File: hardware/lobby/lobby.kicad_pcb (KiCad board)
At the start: 4 copper layers, 85 x 56 mm, 38 parts, among them J1 THD-02-R, J2 THD-20-R, J3 Micro_SD_Card_Det, J4 Conn_01x22_Female, SW1 SW_Push, SW2 SW_SPST, U1 RT9742GGJ5, U2 M.2-keyM, U3 MYLSM00502ERPL, U4 FSUSB42MX

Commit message: update lobby
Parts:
- added H1: MountingHole, MountingHole:MountingHole_2.7mm_M2.5, F.Cu at (69.8, 63.0)
- added H2: MountingHole, MountingHole:MountingHole_2.7mm_M2.5, F.Cu at (100.0, 63.0)
- J3: footprint cm4crypto:SDCARD_MOLEX_503398-1892 -> cm4crypto:amphenol-sd-push-pull_114-00841-68
- R3, R4: value nf -> 2.2K
- R5: value 12K 1% -> nf
- R6: value 2.2k -> nf
- R7: value R -> 12K 1%
- R8: value 2.2K -> 2.2k
- R9: value 2.2K -> R
- moved R8 61.1 mm to (25.0, 31.5)
- moved R6 39.6 mm to (62.0, 45.5), turned to 180 degrees
- moved R3 30.6 mm to (86.0, 28.0), turned to 90 degrees
- moved R4 28.5 mm to (84.5, 28.0), turned to 90 degrees
- moved R9 18.4 mm to (69.8, 39.0), turned to -90 degrees
- moved R7 8.84 mm to (62.0, 43.2), turned to 0 degrees
- moved J3 6.79 mm to (22.8, 47.9), turned to 90 degrees
- moved R5 3.75 mm to (62.0, 47.0), turned to 180 degrees
- moved U2 0.56 mm to (26.2, 63.0)
- moved C10 0.55 mm to (35.5, 72.5)
- moved C4 0.55 mm to (34.0, 72.5)
- moved C5 0.55 mm to (32.5, 72.5)
- moved C11 0.55 mm to (31.0, 72.5)
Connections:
- Module1 pad 100: unconnected-(Module1-Pad100) -> (no net)
- Module1 pad 104: unconnected-(Module1-Pad104) -> (no net)
- Module1 pad 106: unconnected-(Module1-Pad106) -> (no net)
- Module1 pad 111: unconnected-(Module1-Pad111) -> (no net)
- Module1 pad 128: unconnected-(Module1-Pad128) -> (no net)
- Module1 pad 130: unconnected-(Module1-Pad130) -> (no net)
- Module1 pad 134: unconnected-(Module1-Pad134) -> (no net)
- Module1 pad 136: unconnected-(Module1-Pad136) -> (no net)
- Module1 pad 140: unconnected-(Module1-Pad140) -> (no net)
- Module1 pad 142: unconnected-(Module1-Pad142) -> (no net)
- Module1 pad 157: unconnected-(Module1-Pad157) -> (no net)
- Module1 pad 159: unconnected-(Module1-Pad159) -> (no net)
- Module1 pad 16: unconnected-(Module1-Pad16) -> (no net)
- Module1 pad 163: unconnected-(Module1-Pad163) -> (no net)
- Module1 pad 165: unconnected-(Module1-Pad165) -> (no net)
- Module1 pad 169: unconnected-(Module1-Pad169) -> (no net)
- Module1 pad 171: unconnected-(Module1-Pad171) -> (no net)
- Module1 pad 175: unconnected-(Module1-Pad175) -> (no net)
- Module1 pad 177: unconnected-(Module1-Pad177) -> (no net)
- Module1 pad 18: unconnected-(Module1-Pad18) -> (no net)
- Module1 pad 181: unconnected-(Module1-Pad181) -> (no net)
- Module1 pad 183: unconnected-(Module1-Pad183) -> (no net)
- Module1 pad 187: unconnected-(Module1-Pad187) -> (no net)
- Module1 pad 189: unconnected-(Module1-Pad189) -> (no net)
- Module1 pad 19: unconnected-(Module1-Pad19) -> (no net)
- Module1 pad 193: unconnected-(Module1-Pad193) -> (no net)
- Module1 pad 194: unconnected-(Module1-Pad194) -> (no net)
- Module1 pad 195: unconnected-(Module1-Pad195) -> (no net)
- Module1 pad 196: unconnected-(Module1-Pad196) -> (no net)
- Module1 pad 24: /GPIO26 -> (no net)
- Module1 pad 25: /GPIO21 -> (no net)
- Module1 pad 26: /GPIO19 -> (no net)
- Module1 pad 27: /GPIO20 -> (no net)
- Module1 pad 28: /GPIO13 -> (no net)
- Module1 pad 29: /GPIO16 -> (no net)
- Module1 pad 30: /GPIO6 -> (no net)
- Module1 pad 31: /GPIO12 -> (no net)
- Module1 pad 34: /GPIO5 -> (no net)
- Module1 pad 35: /ID_SC -> (no net)
- Module1 pad 36: /ID_SD -> (no net)
- Module1 pad 37: /GPIO7 -> (no net)
- Module1 pad 38: /GPIO11 -> (no net)
- Module1 pad 39: /GPIO8 -> (no net)
- Module1 pad 40: /GPIO9 -> (no net)
- Module1 pad 41: /GPIO25 -> (no net)
- Module1 pad 44: /GPIO10 -> (no net)
- Module1 pad 45: /GPIO24 -> (no net)
- Module1 pad 46: /GPIO22 -> (no net)
- Module1 pad 47: /GPIO23 -> (no net)
- Module1 pad 48: /GPIO27 -> (no net)
- Module1 pad 49: /GPIO18 -> (no net)
- Module1 pad 50: /GPIO17 -> (no net)
- Module1 pad 51: /GPIO15 -> (no net)
- Module1 pad 54: /GPIO4 -> (no net)
- Module1 pad 64: unconnected-(Module1-Pad64) -> (no net)
- Module1 pad 68: unconnected-(Module1-Pad68) -> (no net)
- Module1 pad 70: unconnected-(Module1-Pad70) -> (no net)
- Module1 pad 72: unconnected-(Module1-Pad72) -> (no net)
- Module1 pad 73: unconnected-(Module1-Pad73) -> (no net)
- Module1 pad 76: unconnected-(Module1-Pad76) -> (no net)
- Module1 pad 84: unconnected-(Module1-Pad84) -> (no net)
- Module1 pad 86: unconnected-(Module1-Pad86) -> (no net)
- Module1 pad 92: unconnected-(Module1-Pad92) -> (no net)
- Module1 pad 99: unconnected-(Module1-Pad99) -> (no net)
- R3 pad 1: /+3.3v -> /GPIO_VREF
- R3 pad 2: Net-(J3-Pad10) -> /GPIO2
- R4 pad 1: (no net) -> /GPIO_VREF
- R4 pad 2: Net-(J3-Pad9) -> /GPIO3
- R5 pad 2: /SD_PWR_ON -> Net-(J3-Pad10)
- R6 pad 1: /USBOTG_ID -> (no net)
- R6 pad 2: GND -> Net-(J3-Pad9)
- R7 pad 1: Net-(R7-Pad1) -> /+3.3v
- R7 pad 2: GND -> /SD_PWR_ON
- R8 pad 1: /GPIO_VREF -> /USBOTG_ID
- R8 pad 2: /GPIO2 -> GND
- R9 pad 1: /GPIO_VREF -> Net-(R9-Pad1)
- R9 pad 2: /GPIO3 -> GND
- U3 pad 1: Net-(R7-Pad1) -> Net-(R9-Pad1)
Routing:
- net GND: track 148.5 -> 126.0 mm, vias 195 -> 187
- net Net-(R7-Pad1): track 17.0 -> 0.00 mm, vias 2 -> 0
- net Net-(R9-Pad1): track 0.00 -> 16.8 mm, vias 0 -> 2
- net /+3.3v: track 240.5 -> 230.4 mm, vias 10 -> 13
- net Net-(J3-Pad10): track 33.9 -> 42.8 mm
- net /TR1_TAP: track 63.2 -> 71.6 mm
- net Net-(J3-Pad9): track 30.6 -> 38.3 mm
- net /TR0_TAP: track 78.5 -> 85.9 mm
- net /TR2_TAP: track 72.9 -> 80.1 mm
- net /SD_DAT0: track 72.2 -> 79.1 mm
- net /TR3_TAP: track 79.5 -> 83.6 mm
- net /+5v: track 167.8 -> 171.8 mm
- net /SD_CLK: track 65.2 -> 69.0 mm
- net /SD_DAT2: track 69.2 -> 72.9 mm
- net /sd/SD_PWR: track 50.8 -> 47.6 mm
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- added copper zone on B.Cu, net /+3.3v

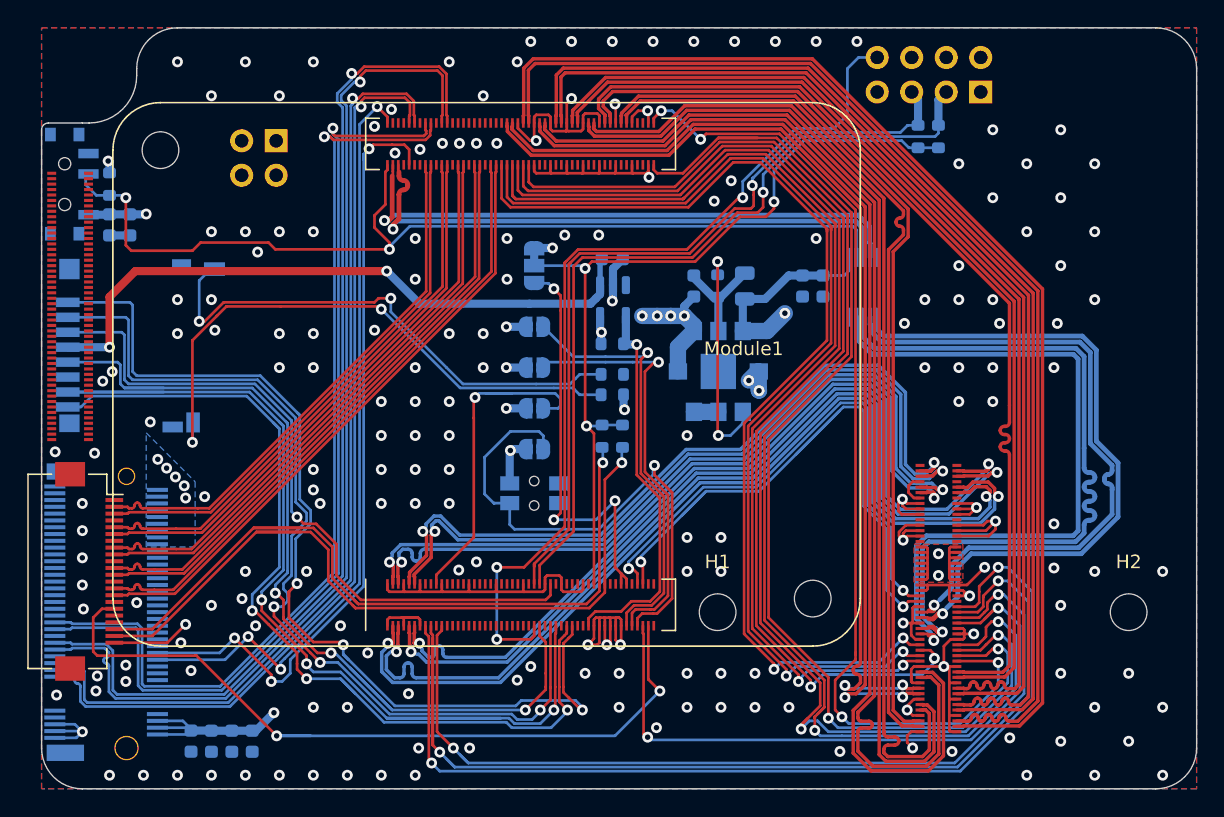
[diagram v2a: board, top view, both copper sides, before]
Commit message: mirror lobby mezzanine connector
fixing a big whoops
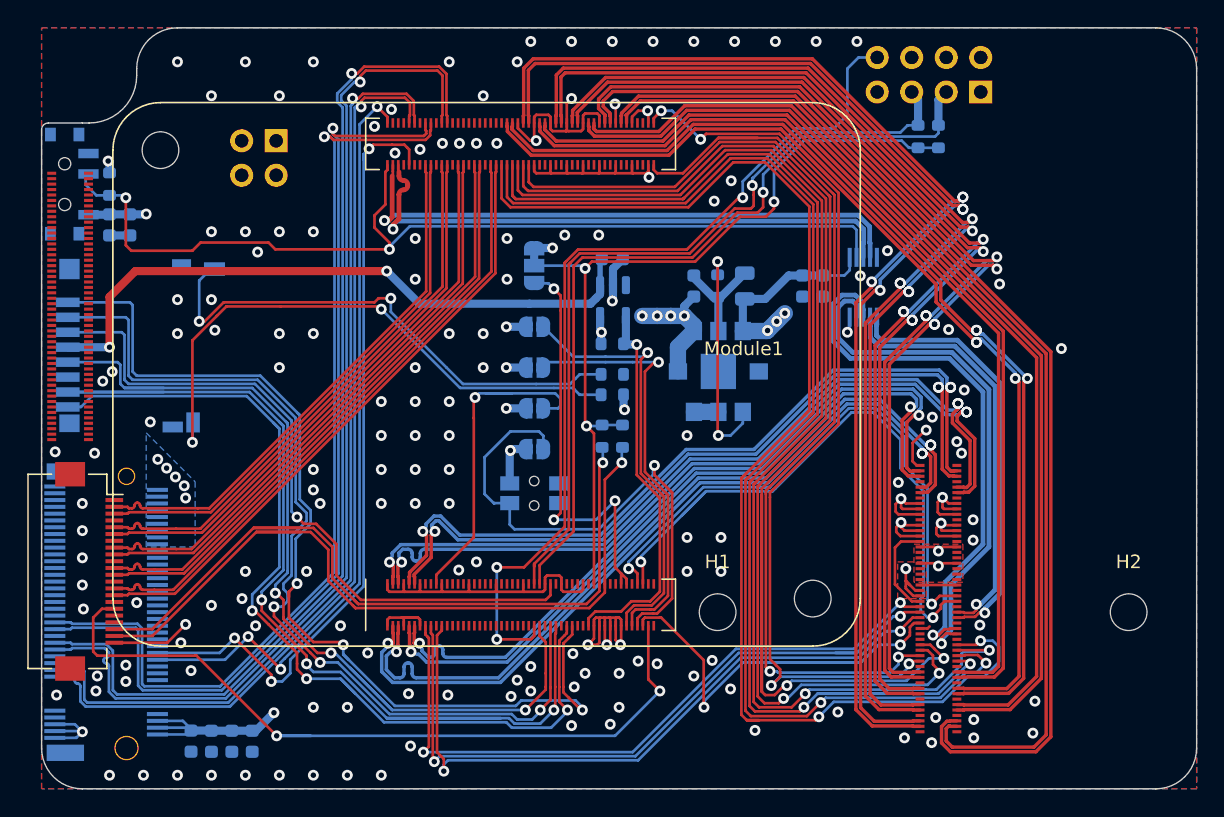
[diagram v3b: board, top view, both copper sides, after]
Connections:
- J4 pad 18: (no net) -> unconnected-(J4-Pad18)
- Module1 pad 100: (no net) -> unconnected-(Module1-Pad100)
- Module1 pad 104: (no net) -> unconnected-(Module1-Pad104)
- Module1 pad 106: (no net) -> unconnected-(Module1-Pad106)
- Module1 pad 111: (no net) -> unconnected-(Module1-Pad111)
- Module1 pad 128: (no net) -> unconnected-(Module1-Pad128)
- Module1 pad 130: (no net) -> unconnected-(Module1-Pad130)
- Module1 pad 134: (no net) -> unconnected-(Module1-Pad134)
- Module1 pad 136: (no net) -> unconnected-(Module1-Pad136)
- Module1 pad 140: (no net) -> unconnected-(Module1-Pad140)
- Module1 pad 142: (no net) -> unconnected-(Module1-Pad142)
- Module1 pad 157: (no net) -> unconnected-(Module1-Pad157)
- Module1 pad 159: (no net) -> unconnected-(Module1-Pad159)
- Module1 pad 16: (no net) -> unconnected-(Module1-Pad16)
- Module1 pad 163: (no net) -> unconnected-(Module1-Pad163)
- Module1 pad 165: (no net) -> unconnected-(Module1-Pad165)
- Module1 pad 169: (no net) -> unconnected-(Module1-Pad169)
- Module1 pad 171: (no net) -> unconnected-(Module1-Pad171)
- Module1 pad 175: (no net) -> unconnected-(Module1-Pad175)
- Module1 pad 177: (no net) -> unconnected-(Module1-Pad177)
- Module1 pad 18: (no net) -> unconnected-(Module1-Pad18)
- Module1 pad 181: (no net) -> unconnected-(Module1-Pad181)
- Module1 pad 183: (no net) -> unconnected-(Module1-Pad183)
- Module1 pad 187: (no net) -> unconnected-(Module1-Pad187)
- Module1 pad 189: (no net) -> unconnected-(Module1-Pad189)
- Module1 pad 19: (no net) -> unconnected-(Module1-Pad19)
- Module1 pad 193: (no net) -> unconnected-(Module1-Pad193)
- Module1 pad 194: (no net) -> unconnected-(Module1-Pad194)
- Module1 pad 195: (no net) -> unconnected-(Module1-Pad195)
- Module1 pad 196: (no net) -> unconnected-(Module1-Pad196)
- Module1 pad 24: (no net) -> /GPIO26
- Module1 pad 25: (no net) -> /GPIO21
- Module1 pad 26: (no net) -> /GPIO19
- Module1 pad 27: (no net) -> /GPIO20
- Module1 pad 28: (no net) -> /GPIO13
- Module1 pad 29: (no net) -> /GPIO16
- Module1 pad 30: (no net) -> /GPIO6
- Module1 pad 31: (no net) -> /GPIO12
- Module1 pad 34: (no net) -> /GPIO5
- Module1 pad 35: (no net) -> /ID_SC
- Module1 pad 36: (no net) -> /ID_SD
- Module1 pad 37: (no net) -> /GPIO7
- Module1 pad 38: (no net) -> /GPIO11
- Module1 pad 39: (no net) -> /GPIO8
- Module1 pad 40: (no net) -> /GPIO9
- Module1 pad 41: (no net) -> /GPIO25
- Module1 pad 44: (no net) -> /GPIO10
- Module1 pad 45: (no net) -> /GPIO24
- Module1 pad 46: (no net) -> /GPIO22
- Module1 pad 47: (no net) -> /GPIO23
- Module1 pad 48: (no net) -> /GPIO27
- Module1 pad 49: (no net) -> /GPIO18
- Module1 pad 50: (no net) -> /GPIO17
- Module1 pad 51: (no net) -> /GPIO15
- Module1 pad 54: (no net) -> /GPIO4
- Module1 pad 64: (no net) -> unconnected-(Module1-Pad64)
- Module1 pad 68: (no net) -> unconnected-(Module1-Pad68)
- Module1 pad 70: (no net) -> unconnected-(Module1-Pad70)
- Module1 pad 72: (no net) -> unconnected-(Module1-Pad72)
- Module1 pad 73: (no net) -> unconnected-(Module1-Pad73)
- Module1 pad 76: (no net) -> unconnected-(Module1-Pad76)
- Module1 pad 84: (no net) -> unconnected-(Module1-Pad84)
- Module1 pad 86: (no net) -> unconnected-(Module1-Pad86)
- Module1 pad 92: (no net) -> unconnected-(Module1-Pad92)
- Module1 pad 99: (no net) -> unconnected-(Module1-Pad99)
- Module2 pad 10: /TRD3_P -> /TRD1_P
- Module2 pad 11: /TRD1_N -> /TRD3_N
- Module2 pad 12: /TRD3_N -> /TRD1_N
- Module2 pad 15: /TR1_TAP -> /TR3_TAP
- Module2 pad 16: /TR3_TAP -> /TR1_TAP
- Module2 pad 17: /TR1_TAP -> /TR3_TAP
- Module2 pad 18: /TR3_TAP -> /TR1_TAP
- Module2 pad 19: /TR1_TAP -> /TR3_TAP
- Module2 pad 20: /TR3_TAP -> /TR1_TAP
- Module2 pad 23: /TR2_TAP -> /TR0_TAP
- Module2 pad 24: /TR0_TAP -> /TR2_TAP
- Module2 pad 25: /TR2_TAP -> /TR0_TAP
- Module2 pad 26: /TR0_TAP -> /TR2_TAP
- Module2 pad 27: /TR2_TAP -> /TR0_TAP
- Module2 pad 28: /TR0_TAP -> /TR2_TAP
- Module2 pad 3: /TRD0_N -> /TRD2_P
- Module2 pad 4: /TRD2_P -> /TRD0_N
- Module2 pad 47: GND -> /+3.3v
- Module2 pad 48: /+3.3v -> GND
- Module2 pad 49: /AnalogIP1 -> /+3.3v
- Module2 pad 5: /TRD0_P -> /TRD2_N
- Module2 pad 50: /+3.3v -> /AnalogIP1
- Module2 pad 51: /AnalogIP0 -> GND
- Module2 pad 52: GND -> /AnalogIP0
- Module2 pad 53: GND -> /ETH_LEDY
- Module2 pad 54: /ETH_LEDY -> GND
- Module2 pad 55: /USB2_HOST_P -> /ETH_LEDG
- Module2 pad 56: /ETH_LEDG -> /USB2_HOST_P
- Module2 pad 57: /USB2_HOST_N -> /nPI_LED_ACTIVITY
- Module2 pad 58: /nPI_LED_ACTIVITY -> /USB2_HOST_N
- Module2 pad 59: GND -> /nPI_LED_PWR
- Module2 pad 6: /TRD2_N -> /TRD0_P
- Module2 pad 60: /nPI_LED_PWR -> GND
- Module2 pad 61: /USB2_DEV_N -> GND
- Module2 pad 62: GND -> /USB2_DEV_N
- Module2 pad 63: /USB2_DEV_P -> GND
- Module2 pad 64: GND -> /USB2_DEV_P
- Module2 pad 67: /HDMI1_HOTPLUG -> /HDMI0_HOTPLUG
- Module2 pad 68: /HDMI0_HOTPLUG -> /HDMI1_HOTPLUG
- Module2 pad 69: /HDMI1_CEC -> /HDMI0_CEC
- Module2 pad 70: /HDMI0_CEC -> /HDMI1_CEC
- Module2 pad 71: /HDMI1_SDA -> /HDMI0_SDA
- Module2 pad 72: /HDMI0_SDA -> /HDMI1_SDA
- Module2 pad 73: /HDMI1_SCL -> /HDMI0_SCL
- Module2 pad 74: /HDMI0_SCL -> /HDMI1_SCL
- Module2 pad 77: /HDMI1_TX0_P -> /HDMI0_TX0_N
- Module2 pad 78: /HDMI0_TX0_N -> /HDMI1_TX0_P
- Module2 pad 79: /HDMI1_TX0_N -> /HDMI0_TX0_P
- Module2 pad 80: /HDMI0_TX0_P -> /HDMI1_TX0_N
- Module2 pad 83: /HDMI1_TX2_P -> /HDMI0_TX2_N
- Module2 pad 84: /HDMI0_TX2_N -> /HDMI1_TX2_P
- Module2 pad 85: /HDMI1_TX2_N -> /HDMI0_TX2_P
- Module2 pad 86: /HDMI0_TX2_P -> /HDMI1_TX2_N
- Module2 pad 89: /HDMI0_TX1_P -> /HDMI1_CLK_N
- Module2 pad 9: /TRD1_P -> /TRD3_P
- Module2 pad 90: /HDMI1_CLK_N -> /HDMI0_TX1_P
- Module2 pad 91: /HDMI0_TX1_N -> /HDMI1_CLK_P
- Module2 pad 92: /HDMI1_CLK_P -> /HDMI0_TX1_N
- Module2 pad 95: /HDMI0_CLK_P -> /HDMI1_TX1_N
- Module2 pad 96: /HDMI1_TX1_N -> /HDMI0_CLK_P
- Module2 pad 97: /HDMI0_CLK_N -> /HDMI1_TX1_P
- Module2 pad 98: /HDMI1_TX1_P -> /HDMI0_CLK_N
- Module3 pad 1: (no net) -> unconnected-(Module3-Pad1)
- Module3 pad 10: (no net) -> unconnected-(Module3-Pad10)
- Module3 pad 100: (no net) -> unconnected-(Module3-Pad100)
- Module3 pad 11: (no net) -> unconnected-(Module3-Pad11)
- Module3 pad 12: (no net) -> unconnected-(Module3-Pad12)
- Module3 pad 13: (no net) -> unconnected-(Module3-Pad13)
- Module3 pad 14: (no net) -> unconnected-(Module3-Pad14)
- Module3 pad 15: (no net) -> unconnected-(Module3-Pad15)
- Module3 pad 16: (no net) -> unconnected-(Module3-Pad16)
- Module3 pad 17: (no net) -> unconnected-(Module3-Pad17)
- Module3 pad 18: (no net) -> unconnected-(Module3-Pad18)
- Module3 pad 19: (no net) -> unconnected-(Module3-Pad19)
- Module3 pad 2: (no net) -> unconnected-(Module3-Pad2)
- Module3 pad 20: (no net) -> unconnected-(Module3-Pad20)
- Module3 pad 21: (no net) -> unconnected-(Module3-Pad21)
- Module3 pad 22: (no net) -> unconnected-(Module3-Pad22)
- Module3 pad 23: (no net) -> unconnected-(Module3-Pad23)
- Module3 pad 24: (no net) -> unconnected-(Module3-Pad24)
- Module3 pad 25: (no net) -> unconnected-(Module3-Pad25)
- Module3 pad 26: (no net) -> unconnected-(Module3-Pad26)
- Module3 pad 27: (no net) -> unconnected-(Module3-Pad27)
- Module3 pad 28: (no net) -> unconnected-(Module3-Pad28)
- Module3 pad 29: (no net) -> unconnected-(Module3-Pad29)
- Module3 pad 3: (no net) -> unconnected-(Module3-Pad3)
- Module3 pad 30: (no net) -> unconnected-(Module3-Pad30)
- Module3 pad 31: (no net) -> unconnected-(Module3-Pad31)
- Module3 pad 32: (no net) -> unconnected-(Module3-Pad32)
- Module3 pad 33: (no net) -> unconnected-(Module3-Pad33)
- Module3 pad 34: (no net) -> unconnected-(Module3-Pad34)
- Module3 pad 35: (no net) -> unconnected-(Module3-Pad35)
- Module3 pad 36: (no net) -> unconnected-(Module3-Pad36)
- Module3 pad 37: (no net) -> unconnected-(Module3-Pad37)
- Module3 pad 38: (no net) -> unconnected-(Module3-Pad38)
- Module3 pad 39: (no net) -> unconnected-(Module3-Pad39)
- Module3 pad 4: (no net) -> unconnected-(Module3-Pad4)
- Module3 pad 40: (no net) -> unconnected-(Module3-Pad40)
- Module3 pad 41: (no net) -> unconnected-(Module3-Pad41)
- Module3 pad 42: (no net) -> unconnected-(Module3-Pad42)
- Module3 pad 43: (no net) -> unconnected-(Module3-Pad43)
- Module3 pad 44: (no net) -> unconnected-(Module3-Pad44)
- Module3 pad 45: (no net) -> unconnected-(Module3-Pad45)
- Module3 pad 46: (no net) -> unconnected-(Module3-Pad46)
- Module3 pad 47: (no net) -> unconnected-(Module3-Pad47)
- Module3 pad 48: (no net) -> unconnected-(Module3-Pad48)
- Module3 pad 49: (no net) -> unconnected-(Module3-Pad49)
- Module3 pad 5: (no net) -> unconnected-(Module3-Pad5)
- Module3 pad 50: (no net) -> unconnected-(Module3-Pad50)
- Module3 pad 51: (no net) -> unconnected-(Module3-Pad51)
- Module3 pad 52: (no net) -> unconnected-(Module3-Pad52)
- Module3 pad 53: (no net) -> unconnected-(Module3-Pad53)
- Module3 pad 54: (no net) -> unconnected-(Module3-Pad54)
- Module3 pad 55: (no net) -> unconnected-(Module3-Pad55)
- Module3 pad 56: (no net) -> unconnected-(Module3-Pad56)
- Module3 pad 57: (no net) -> unconnected-(Module3-Pad57)
- Module3 pad 58: (no net) -> unconnected-(Module3-Pad58)
- Module3 pad 59: (no net) -> unconnected-(Module3-Pad59)
- Module3 pad 6: (no net) -> unconnected-(Module3-Pad6)
- Module3 pad 60: (no net) -> unconnected-(Module3-Pad60)
- Module3 pad 61: (no net) -> unconnected-(Module3-Pad61)
- Module3 pad 62: (no net) -> unconnected-(Module3-Pad62)
- Module3 pad 63: (no net) -> unconnected-(Module3-Pad63)
- Module3 pad 64: (no net) -> unconnected-(Module3-Pad64)
- Module3 pad 65: (no net) -> unconnected-(Module3-Pad65)
- Module3 pad 66: (no net) -> unconnected-(Module3-Pad66)
- Module3 pad 67: (no net) -> unconnected-(Module3-Pad67)
- Module3 pad 68: (no net) -> unconnected-(Module3-Pad68)
- Module3 pad 69: (no net) -> unconnected-(Module3-Pad69)
- Module3 pad 7: (no net) -> unconnected-(Module3-Pad7)
- Module3 pad 70: (no net) -> unconnected-(Module3-Pad70)
- Module3 pad 71: (no net) -> unconnected-(Module3-Pad71)
- Module3 pad 72: (no net) -> unconnected-(Module3-Pad72)
- Module3 pad 73: (no net) -> unconnected-(Module3-Pad73)
- Module3 pad 74: (no net) -> unconnected-(Module3-Pad74)
- Module3 pad 75: (no net) -> unconnected-(Module3-Pad75)
- Module3 pad 76: (no net) -> unconnected-(Module3-Pad76)
- Module3 pad 77: (no net) -> unconnected-(Module3-Pad77)
- Module3 pad 78: (no net) -> unconnected-(Module3-Pad78)
- Module3 pad 79: (no net) -> unconnected-(Module3-Pad79)
- Module3 pad 8: (no net) -> unconnected-(Module3-Pad8)
- Module3 pad 80: (no net) -> unconnected-(Module3-Pad80)
- Module3 pad 81: (no net) -> unconnected-(Module3-Pad81)
- Module3 pad 82: (no net) -> unconnected-(Module3-Pad82)
- Module3 pad 83: (no net) -> unconnected-(Module3-Pad83)
- Module3 pad 84: (no net) -> unconnected-(Module3-Pad84)
- Module3 pad 85: (no net) -> unconnected-(Module3-Pad85)
- Module3 pad 86: (no net) -> unconnected-(Module3-Pad86)
- Module3 pad 87: (no net) -> unconnected-(Module3-Pad87)
- Module3 pad 88: (no net) -> unconnected-(Module3-Pad88)
- Module3 pad 89: (no net) -> unconnected-(Module3-Pad89)
- Module3 pad 9: (no net) -> unconnected-(Module3-Pad9)
- Module3 pad 90: (no net) -> unconnected-(Module3-Pad90)
- Module3 pad 91: (no net) -> unconnected-(Module3-Pad91)
- Module3 pad 92: (no net) -> unconnected-(Module3-Pad92)
- Module3 pad 93: (no net) -> unconnected-(Module3-Pad93)
- Module3 pad 94: (no net) -> unconnected-(Module3-Pad94)
- Module3 pad 95: (no net) -> unconnected-(Module3-Pad95)
- Module3 pad 96: (no net) -> unconnected-(Module3-Pad96)
- Module3 pad 97: (no net) -> unconnected-(Module3-Pad97)
- Module3 pad 98: (no net) -> unconnected-(Module3-Pad98)
- Module3 pad 99: (no net) -> unconnected-(Module3-Pad99)
- R6 pad 1: (no net) -> /sd/Reserved
- U1 pad 3: (no net) -> unconnected-(U1-Pad3)
- U2 pad 10: (no net) -> unconnected-(U2-Pad10)
- U2 pad 11: (no net) -> unconnected-(U2-Pad11)
- U2 pad 13: (no net) -> unconnected-(U2-Pad13)
- U2 pad 17: (no net) -> unconnected-(U2-Pad17)
- U2 pad 19: (no net) -> unconnected-(U2-Pad19)
- U2 pad 20: (no net) -> unconnected-(U2-Pad20)
- U2 pad 22: (no net) -> unconnected-(U2-Pad22)
- U2 pad 23: (no net) -> unconnected-(U2-Pad23)
- U2 pad 24: (no net) -> unconnected-(U2-Pad24)
- U2 pad 25: (no net) -> unconnected-(U2-Pad25)
- U2 pad 26: (no net) -> unconnected-(U2-Pad26)
- U2 pad 28: (no net) -> unconnected-(U2-Pad28)
- U2 pad 29: (no net) -> unconnected-(U2-Pad29)
- U2 pad 30: (no net) -> unconnected-(U2-Pad30)
- U2 pad 31: (no net) -> unconnected-(U2-Pad31)
- U2 pad 32: (no net) -> unconnected-(U2-Pad32)
- U2 pad 34: (no net) -> unconnected-(U2-Pad34)
- U2 pad 35: (no net) -> unconnected-(U2-Pad35)
- U2 pad 36: (no net) -> unconnected-(U2-Pad36)
- U2 pad 37: (no net) -> unconnected-(U2-Pad37)
- U2 pad 38: (no net) -> unconnected-(U2-Pad38)
- U2 pad 40: (no net) -> unconnected-(U2-Pad40)
- U2 pad 42: (no net) -> unconnected-(U2-Pad42)
- U2 pad 44: (no net) -> unconnected-(U2-Pad44)
- U2 pad 46: (no net) -> unconnected-(U2-Pad46)
- U2 pad 48: (no net) -> unconnected-(U2-Pad48)
- U2 pad 5: (no net) -> unconnected-(U2-Pad5)
- U2 pad 54: (no net) -> unconnected-(U2-Pad54)
- U2 pad 56: (no net) -> unconnected-(U2-Pad56)
- U2 pad 58: (no net) -> unconnected-(U2-Pad58)
- U2 pad 6: (no net) -> unconnected-(U2-Pad6)
- U2 pad 67: (no net) -> unconnected-(U2-Pad67)
- U2 pad 68: (no net) -> unconnected-(U2-Pad68)
- U2 pad 69: (no net) -> unconnected-(U2-Pad69)
- U2 pad 7: (no net) -> unconnected-(U2-Pad7)
- U2 pad 8: (no net) -> unconnected-(U2-Pad8)
- U3 pad 8: /+5v -> GND
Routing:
- net /ETH_LEDG: track 78.5 -> 52.1 mm
- net GND: track 126.0 -> 103.3 mm, vias 187 -> 162
- net /ETH_LEDY: track 73.0 -> 50.8 mm
- net /USB2_HOST_P: track 49.6 -> 31.0 mm
- net /USB2_HOST_N: track 49.9 -> 31.6 mm
- net /HDMI1_HOTPLUG: track 78.0 -> 95.5 mm
- net /HDMI1_SCL: track 77.4 -> 93.9 mm
- net /HDMI0_SDA: track 84.5 -> 68.7 mm
- net /nPI_LED_ACTIVITY: track 67.4 -> 51.5 mm
- net /TR0_TAP: track 85.9 -> 71.1 mm
- net /HDMI0_CEC: track 97.9 -> 83.1 mm
- net /HDMI0_CLK_P: track 65.5 -> 80.2 mm
- net /HDMI1_TX0_P: track 84.7 -> 69.9 mm
- net /USB2_DEV_N: track 55.4 -> 40.7 mm
- net /HDMI1_TX0_N: track 84.6 -> 70.5 mm
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- added copper zone on F.Cu, net /+3.3v

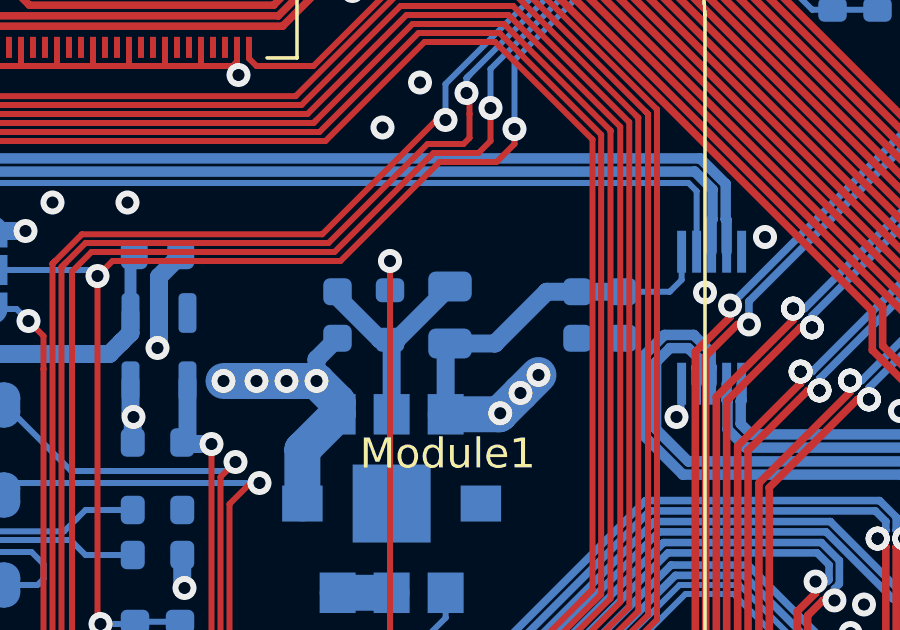
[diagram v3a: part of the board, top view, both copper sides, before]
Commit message: modify footprints
add paste on hdmi and usbc
add silkscreen outline on murata dcdc supply
change PS cap footprint to polarized footprint
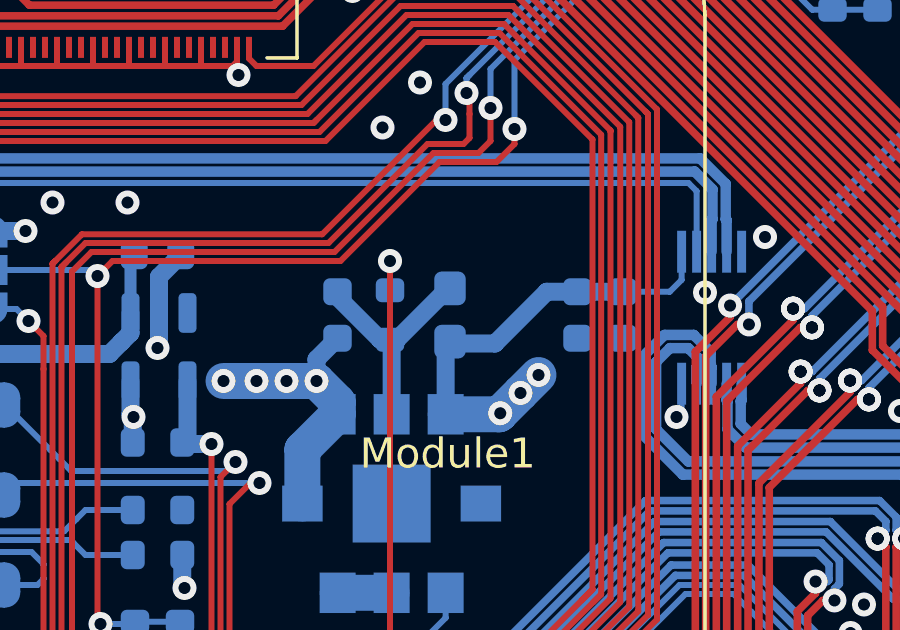
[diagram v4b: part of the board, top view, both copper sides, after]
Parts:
- C6: footprint Capacitor_SMD:C_0805_2012Metric -> Capacitor_Tantalum_SMD:CP_EIA-2012-15_AVX-P
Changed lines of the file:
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@@
     )
   )
-  (footprint "Capacitor_SMD:C_0805_2012Metric" (layer "B.Cu")
+  (footprint "Capacitor_Tantalum_SMD:CP_EIA-2012-15_AVX-P" (layer "B.Cu")
     (at 71.75 39 90)
-    (descr "Capacitor SMD 0805 (2012 Metric), square (rectangular) end terminal, IPC_7351 nominal, (Body size source: IPC-SM-782 page 76, https://www.pcb-3d.com/wordpress/wp-content/uploads/ipc-sm-782a_amendment_1_and_2.pdf, https://docs.google.com/spreadsheets/d/1BsfQQcO9C6DZCsRaXUlFlo91Tg2WpOkGARC1WS5S8t0/edit?usp=sharing), generated with kicad-footprint-generator")
-    (tags "capacitor")
+    (descr "Tantalum Capacitor SMD AVX-P (2012-15 Metric), IPC_7351 nominal, (Body size from: https://www.vishay.com/docs/40182/tmch.pdf), generated with kicad-footprint-generator")
+    (tags "capacitor tantalum")
     (property "Sheetfile" "./sheets/power.kicad_sch")
     (property "Sheetname" "power")
     (attr smd)
-    (fp_text reference "C6" (at 0 1.68 90) (layer "B.SilkS") hide
+    (fp_text reference "C6" (at 0 1.58 270) (layer "B.SilkS")
       (effects (font (size 1 1) (thickness 0.15)) (justify mirror))
     )
-    (fp_text value "47 uF / 6.3V" (at 7.1 -0.05 90) (layer "B.Fab")
+    (fp_text value "47 uF / 6.3V" (at 0 -1.58 270) (layer "B.Fab")
       (effects (font (size 1 1) (thickness 0.15)) (justify mirror))
     )
@@
       (effects (font (size 0.5 0.5) (thickness 0.08)) (justify mirror))
     )
-    (fp_line (start -0.261252 -0.735) (end 0.261252 -0.735) (layer "B.SilkS") (width 0.12))
-    (fp_line (start -0.261252 0.735) (end 0.261252 0.735) (layer "B.SilkS") (width 0.12))
-    (fp_line (start -1.7 -0.98) (end -1.7 0.98) (layer "B.CrtYd") (width 0.05))
-    (fp_line (start 1.7 0.98) (end 1.7 -0.98) (layer "B.CrtYd") (width 0.05))
-    (fp_line (start 1.7 -0.98) (end -1.7 -0.98) (layer "B.CrtYd") (width 0.05))
-    (fp_line (start -1.7 0.98) (end 1.7 0.98) (layer "B.CrtYd") (width 0.05))
-    (fp_line (start 1 0.625) (end 1 -0.625) (layer "B.Fab") (width 0.1))
-    (fp_line (start -1 0.625) (end 1 0.625) (layer "B.Fab") (width 0.1))
-    (fp_line (start 1 -0.625) (end -1 -0.625) (layer "B.Fab") (width 0.1))
-    (fp_line (start -1 -0.625) (end -1 0.625) (layer "B.Fab") (width 0.1))
-    (pad "1" smd roundrect locked (at -0.95 0 90) (size 1 1.45) (layers "B.Cu" "B.Paste" "B.Mask") (roundrect_rratio 0.25)
+    (fp_line (start -1.71 -0.785) (end 1 -0.785) (layer "B.SilkS") (width 0.12))
+    (fp_line (start 1 0.785) (end -1.71 0.785) (layer "B.SilkS") (width 0.12))
+    (fp_line (start -1.71 0.785) (end -1.71 -0.785) (layer "B.SilkS") (width 0.12))
+    (fp_line (start -1.7 -0.88) (end -1.7 0.88) (layer "B.CrtYd") (width 0.05))
+    (fp_line (start 1.7 0.88) (end 1.7 -0.88) (layer "B.CrtYd") (width 0.05))
+    (fp_line (start 1.7 -0.88) (end -1.7 -0.88) (layer "B.CrtYd") (width 0.05))
+    (fp_line (start -1.7 0.88) (end 1.7 0.88) (layer "B.CrtYd") (width 0.05))
+    (fp_line (start 1 0.625) (end -0.6875 0.625) (layer "B.Fab") (width 0.1))
+    (fp_line (start -0.6875 0.625) (end -1 0.3125) (layer "B.Fab") (width 0.1))
+    (fp_line (start 1 -0.625) (end 1 0.625) (layer "B.Fab") (width 0.1))
+    (fp_line (start -1 -0.625) (end 1 -0.625) (layer "B.Fab") (width 0.1))
+    (fp_line (start -1 0.3125) (end -1 -0.625) (layer "B.Fab") (width 0.1))
+    (pad "1" smd roundrect locked (at -0.8875 0 90) (size 1.125 1.05) (layers "B.Cu" "B.Paste" "B.Mask") (roundrect_rratio 0.238095)
       (net 3 "/+3.3v") (pintype "passive"))
-    (pad "2" smd roundrect locked (at 0.95 0 90) (size 1 1.45) (layers "B.Cu" "B.Paste" "B.Mask") (roundrect_rratio 0.25)
+    (pad "2" smd roundrect locked (at 0.8875 0 90) (size 1.125 1.05) (layers "B.Cu" "B.Paste" "B.Mask") (roundrect_rratio 0.238095)
       (net 2 "GND") (pintype "passive"))
-    (model "${KICAD6_3DMODEL_DIR}/Capacitor_SMD.3dshapes/C_0805_2012Metric.wrl"
+    (model "${KICAD6_3DMODEL_DIR}/Capacitor_Tantalum_SMD.3dshapes/CP_EIA-2012-15_AVX-P.wrl"
       (offset (xyz 0 0 0))
       (scale (xyz 1 1 1))
